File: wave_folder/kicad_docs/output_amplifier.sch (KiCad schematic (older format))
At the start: 4 parts, among them U4 TL072

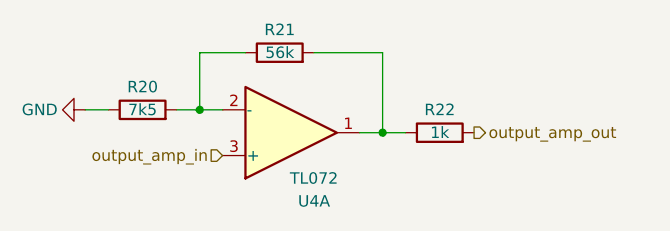
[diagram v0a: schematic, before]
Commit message: small changes to wave folder CV bias and output level
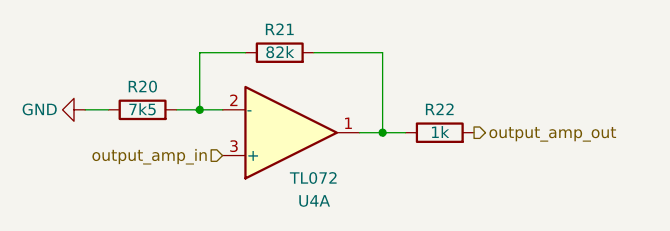
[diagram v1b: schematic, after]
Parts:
- R21: value 56k -> 82k
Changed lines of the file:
@@
 AR Path="/5EF80FC9/5EF833FB" Ref="R21"  Part="1"
 F 0 "R21" V 5800 2900 50  0000 C CNN
-F 1 "56k" V 5700 2900 50  0000 C CNN
+F 1 "82k" V 5700 2900 50  0000 C CNN
 F 2 "Resistor_THT:R_Axial_DIN0207_L6.3mm_D2.5mm_P10.16mm_Horizontal" V 5630 2900 50  0001 C CNN
 F 3 "~" H 5700 2900 50  0001 C CNN
